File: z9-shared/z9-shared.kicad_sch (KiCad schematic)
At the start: 0 parts

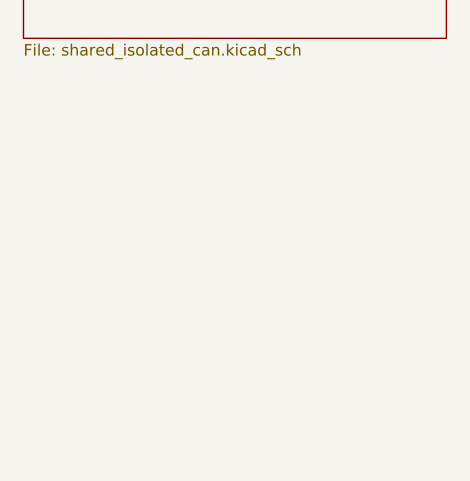
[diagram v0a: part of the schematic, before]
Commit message: Add shared_ism330dhcx schematic and update project configuration - Buzzer chaNGES 3.3v BEADS ANDCAPS - Created a new schematic file for the shared_ism330dhcx component. - Updated the z9-shared project configuration to change the annotation start number from 950 to 700. - Added the shared_ism330dhcx sheet to the main schematic with relevant properties and instances.
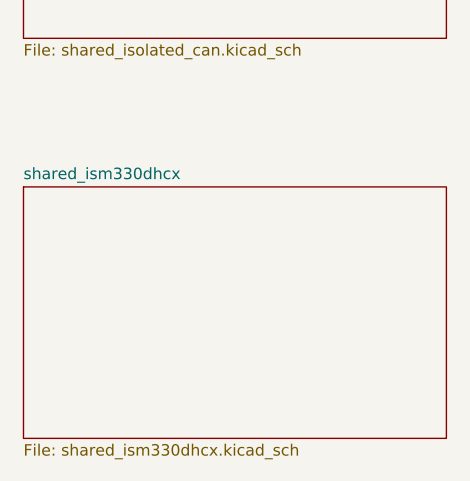
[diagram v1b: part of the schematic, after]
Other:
- added sheet shared_ism330dhcx (shared_ism330dhcx.kicad_sch)
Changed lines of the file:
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@@
+		)
+	)
+	(sheet
+		(at 36.83 147.32)
+		(size 46.99 27.94)
+		(exclude_from_sim no)
+		(in_bom yes)
+		(on_board yes)
+		(dnp no)
+		(fields_autoplaced yes)
+		(stroke
+			(width 0.1524)
+			(type solid)
+		)
+		(fill
+			(color 0 0 0 0.0000)
+		)
+		(property "Sheetname" "shared_ism330dhcx"
+			(at 36.83 146.6084 0)
+			(effects
+				(font
+					(size 1.27 1.27)
+				)
+				(justify left bottom)
+			)
+		)
+		(property "Sheetfile" "shared_ism330dhcx.kicad_sch"
+			(at 36.83 175.8446 0)
+			(effects
+				(font
+					(size 1.27 1.27)
+				)
+				(justify left top)
+			)
+		)
+		(instances
+			(project "z9-shared"
+				(path "/09e08bdc-786f-4949-8afc-e02ddbe0502e"
+					(page "750")
+				)
+			)
 		)
 	)

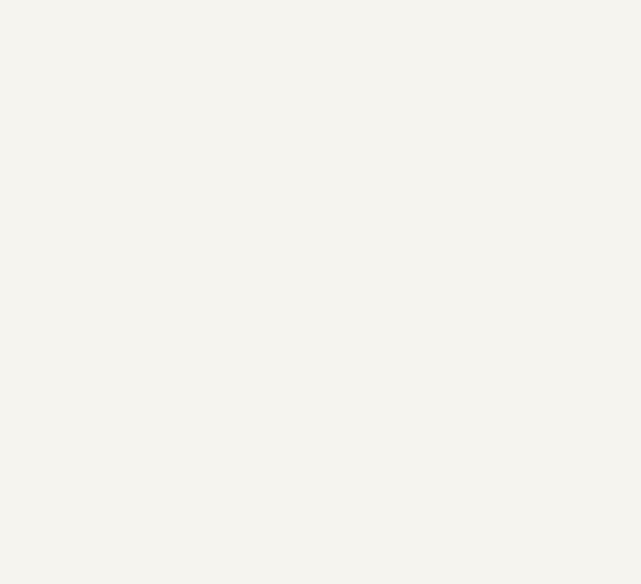
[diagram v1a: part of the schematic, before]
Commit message: Update schematic and project settings for shared components
- Changed the starting annotation number from 700 to 975 in the project configuration.
- Added a new shared schematic sheet named "shared_isolated_can_ps" with relevant properties and instances.
- Included a cautionary text in the schematic to avoid moving components and reannotating to prevent loss of links.
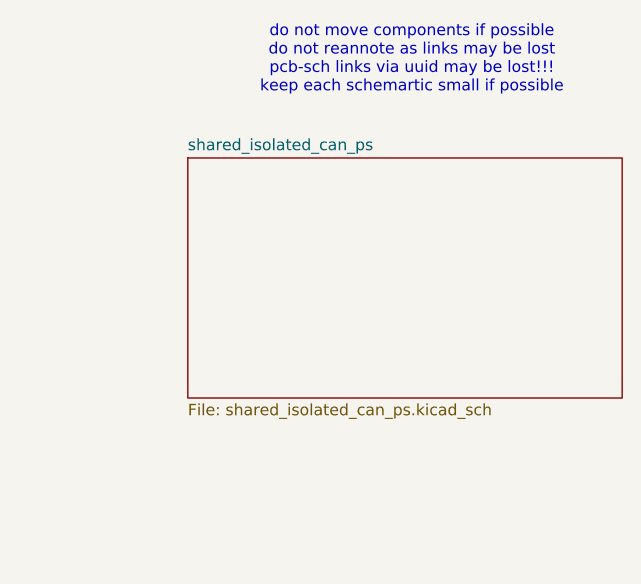
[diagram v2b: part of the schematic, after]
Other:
- added sheet shared_isolated_can_ps (shared_isolated_can_ps.kicad_sch)
- note added: "do not move components if possible do not reannote as links may be lost pcb-sch links via uuid may be lost!!! keep each schemartic small if possible"
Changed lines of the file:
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@@
 	(generator_version "9.0")
 	(paper "A4")
+	(text "do not move components if possible \ndo not reannote as links may be lost\npcb-sch links via uuid may be lost!!!\nkeep each schemartic small if possible "
+		(exclude_from_sim no)
+		(at 169.672 20.828 0)
+		(effects
+			(font
+				(size 1.27 1.27)
+			)
+		)
+	)
 	(no_connect
 		(at 83.82 114.3)
@@
 				)
 			)
+		)
+	)
+	(sheet
+		(at 144.78 31.75)
+		(size 48.26 26.67)
+		(exclude_from_sim no)
+		(in_bom yes)
+		(on_board yes)
+		(dnp no)
+		(fields_autoplaced yes)
+		(stroke
+			(width 0.1524)
+			(type solid)
+		)
+		(fill
+			(color 0 0 0 0.0000)
+		)
+		(property "Sheetname" "shared_isolated_can_ps"
+			(at 144.78 31.0384 0)
+			(effects
+				(font
+					(size 1.27 1.27)
+				)
+				(justify left bottom)
+			)
+		)
+		(property "Sheetfile" "shared_isolated_can_ps.kicad_sch"
+			(at 144.78 59.0046 0)
+			(effects
+				(font
+					(size 1.27 1.27)
+				)
+				(justify left top)
+			)
+		)
+		(instances
+			(project "z9-shared"
+				(path "/09e08bdc-786f-4949-8afc-e02ddbe0502e"
+					(page "7")
+				)
+			)

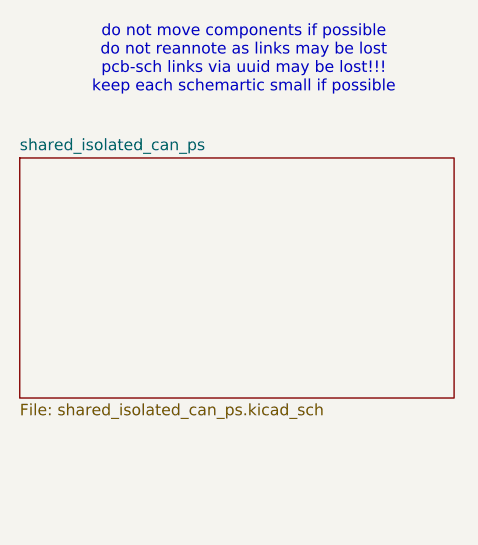
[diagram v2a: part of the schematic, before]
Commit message: Add no-connect pins and ISO power pins to the schematic for shared components
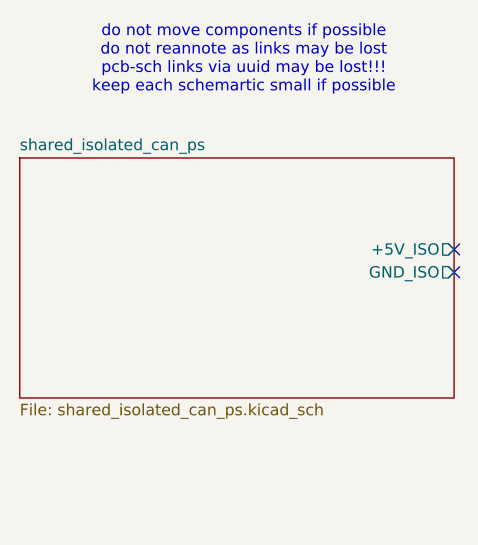
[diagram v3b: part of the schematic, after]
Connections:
- no-connect marks 10 -> 12
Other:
- sheet shared_isolated_can_ps ports: added +5V_ISO, GND_ISO; removed none
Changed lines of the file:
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@@
+	)
+	(no_connect
+		(at 193.04 41.91)
 	)
 	(no_connect
@@
 	(no_connect
 		(at 36.83 43.18)
+	)
+	(no_connect
+		(at 193.04 44.45)
 	)
 	(no_connect
@@
 			)
 		)
+		(pin "+5V_ISO" output
+			(at 193.04 41.91 0)
+			(effects
+				(font
+					(size 1.27 1.27)
+				)
+				(justify right)
+			)
+		)
+		(pin "GND_ISO" output
+			(at 193.04 44.45 0)
+			(effects
+				(font
+					(size 1.27 1.27)
+				)
+				(justify right)
+			)
+		)

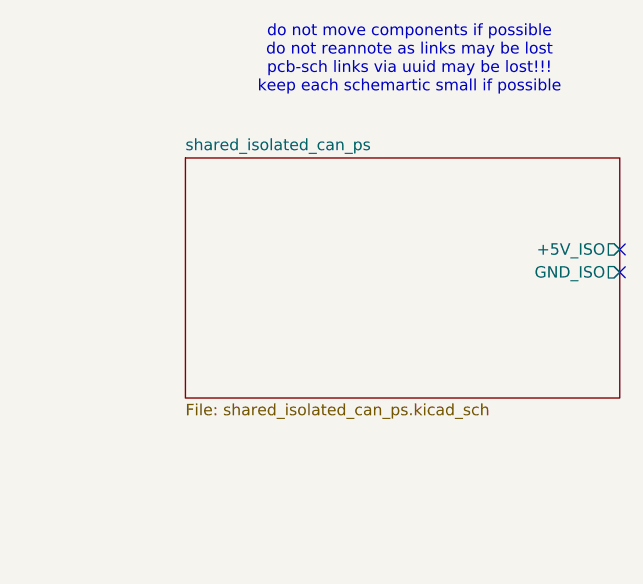
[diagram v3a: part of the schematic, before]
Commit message: Remove unused components and adjust annotation start number in project files
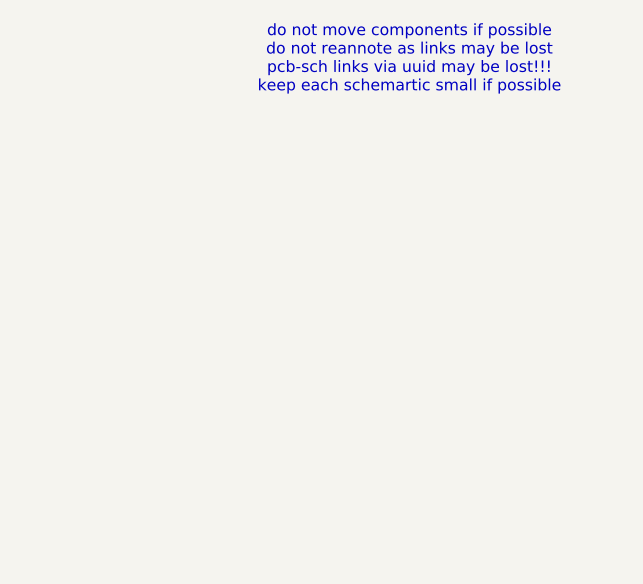
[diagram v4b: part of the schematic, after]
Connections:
- no-connect marks 12 -> 10
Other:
- removed sheet shared_isolated_can_ps
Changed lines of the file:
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@@
-	)
-	(no_connect
-		(at 193.04 41.91)
 	)
 	(no_connect
@@
 	(no_connect
 		(at 36.83 43.18)
-	)
-	(no_connect
-		(at 193.04 44.45)
 	)
 	(no_connect
@@
 				)
 			)
-		)
-	)
-	(sheet
-		(at 144.78 31.75)
-		(size 48.26 26.67)
-		(exclude_from_sim no)
-		(in_bom yes)
-		(on_board yes)
-		(dnp no)
-		(fields_autoplaced yes)
-		(stroke
-			(width 0.1524)
-			(type solid)
-		)
-		(fill
-			(color 0 0 0 0.0000)
-		)
-		(property "Sheetname" "shared_isolated_can_ps"
-			(at 144.78 31.0384 0)
-			(effects
-				(font
-					(size 1.27 1.27)
-				)
-				(justify left bottom)
-			)
-		)
-		(property "Sheetfile" "shared_isolated_can_ps.kicad_sch"
-			(at 144.78 59.0046 0)
-			(effects
-				(font
-					(size 1.27 1.27)
-				)
-				(justify left top)
-			)
-		)
-		(pin "+5V_ISO" output
-			(at 193.04 41.91 0)
-			(effects
-				(font
-					(size 1.27 1.27)
-				)
-				(justify right)
-			)
-		)
-		(pin "GND_ISO" output
-			(at 193.04 44.45 0)
-			(effects
-				(font
-					(size 1.27 1.27)
-				)
-				(justify right)
-			)
-		)
-		(instances
-			(project "z9-shared"
-				(path "/09e08bdc-786f-4949-8afc-e02ddbe0502e"
-					(page "7")
-				)
-			)

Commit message: x
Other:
- added sheet shared_usbc_esp32 (shared_usbc_esp32.kicad_sch)
- sheet shared_ism330dhcx ports: added ISM_CS, ISM_INT1, ISM_INT2, ISM_SCK, ISM_SDI, ISM_SDO; removed none
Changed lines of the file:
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@@
+	)
+	(sheet
+		(at 96.52 31.75)
+		(size 45.72 26.67)
+		(exclude_from_sim no)
+		(in_bom yes)
+		(on_board yes)
+		(dnp no)
+		(fields_autoplaced yes)
+		(stroke
+			(width 0.1524)
+			(type solid)
+		)
+		(fill
+			(color 0 0 0 0.0000)
+		)
+		(property "Sheetname" "shared_usbc_esp32"
+			(at 96.52 31.0384 0)
+			(effects
+				(font
+					(size 1.27 1.27)
+				)
+				(justify left bottom)
+			)
+		)
+		(property "Sheetfile" "shared_usbc_esp32.kicad_sch"
+			(at 96.52 59.0046 0)
+			(effects
+				(font
+					(size 1.27 1.27)
+				)
+				(justify left top)
+			)
+		)
+		(instances
+			(project "z9-shared"
+				(path "/09e08bdc-786f-4949-8afc-e02ddbe0502e"
+					(page "825")
+				)
+			)
+		)
 	)
 	(sheet
@@
 			)
 		)
+		(pin "ISM_CS" input
+			(at 36.83 153.67 180)
+			(effects
+				(font
+					(size 1.27 1.27)
+				)
+				(justify left)
+			)
+		)
+		(pin "ISM_INT1" input
+			(at 36.83 167.64 180)
+			(effects
+				(font
+					(size 1.27 1.27)
+				)
+				(justify left)
+			)
+		)
+		(pin "ISM_INT2" input
+			(at 36.83 170.18 180)
+			(effects
+				(font
+					(size 1.27 1.27)
+				)
+				(justify left)
+			)
+		)
+		(pin "ISM_SCK" input
+			(at 36.83 157.48 180)
+			(effects
+				(font
+					(size 1.27 1.27)
+				)
+				(justify left)
+			)
+		)
+		(pin "ISM_SDI" input
+			(at 36.83 160.02 180)
+			(effects
+				(font
+					(size 1.27 1.27)
+				)
+				(justify left)
+			)
+		)
+		(pin "ISM_SDO" input
+			(at 36.83 162.56 180)
+			(effects
+				(font
+					(size 1.27 1.27)
+				)
+				(justify left)
+			)
+		)

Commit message: pre kicad update
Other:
- added sheet shared_5V_LMR54410 (shared_5V_LMR54410.kicad_sch)
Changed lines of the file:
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@@
+		)
+	)
+	(sheet
+		(at 96.52 71.12)
+		(size 45.72 26.67)
+		(exclude_from_sim no)
+		(in_bom yes)
+		(on_board yes)
+		(dnp no)
+		(fields_autoplaced yes)
+		(stroke
+			(width 0.1524)
+			(type solid)
+		)
+		(fill
+			(color 0 0 0 0.0000)
+		)
+		(property "Sheetname" "shared_5V_LMR54410"
+			(at 96.52 70.4084 0)
+			(effects
+				(font
+					(size 1.27 1.27)
+				)
+				(justify left bottom)
+			)
+		)
+		(property "Sheetfile" "shared_5V_LMR54410.kicad_sch"
+			(at 96.52 98.3746 0)
+			(effects
+				(font
+					(size 1.27 1.27)
+				)
+				(justify left top)
+			)
+		)
+		(instances
+			(project "z9-shared"
+				(path "/09e08bdc-786f-4949-8afc-e02ddbe0502e"
+					(page "600")
+				)
+			)
 		)
 	)

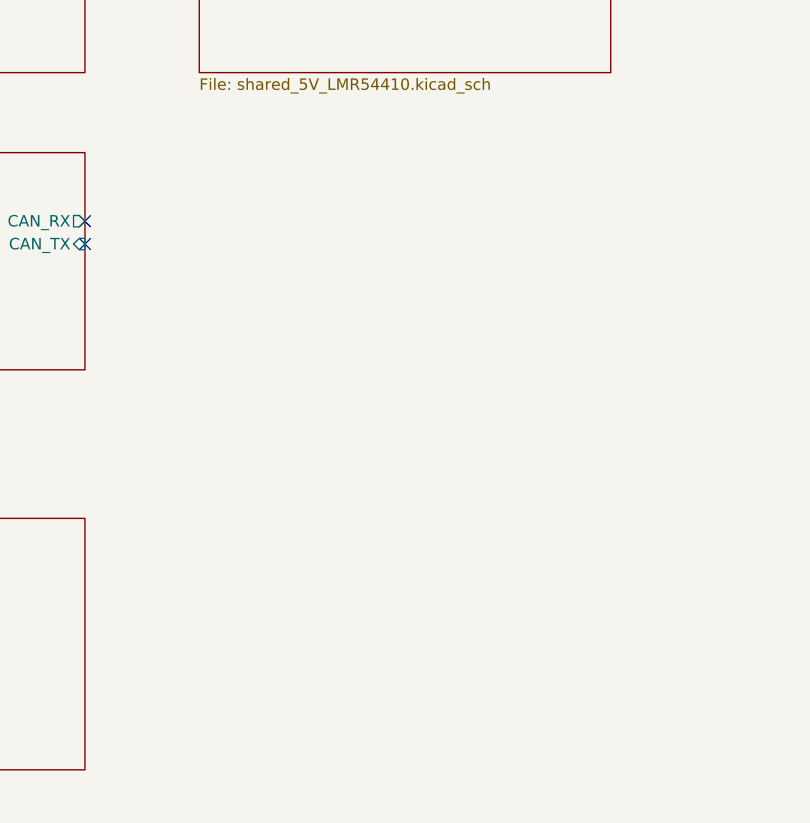
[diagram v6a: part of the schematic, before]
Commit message: new fuse and ideal diode
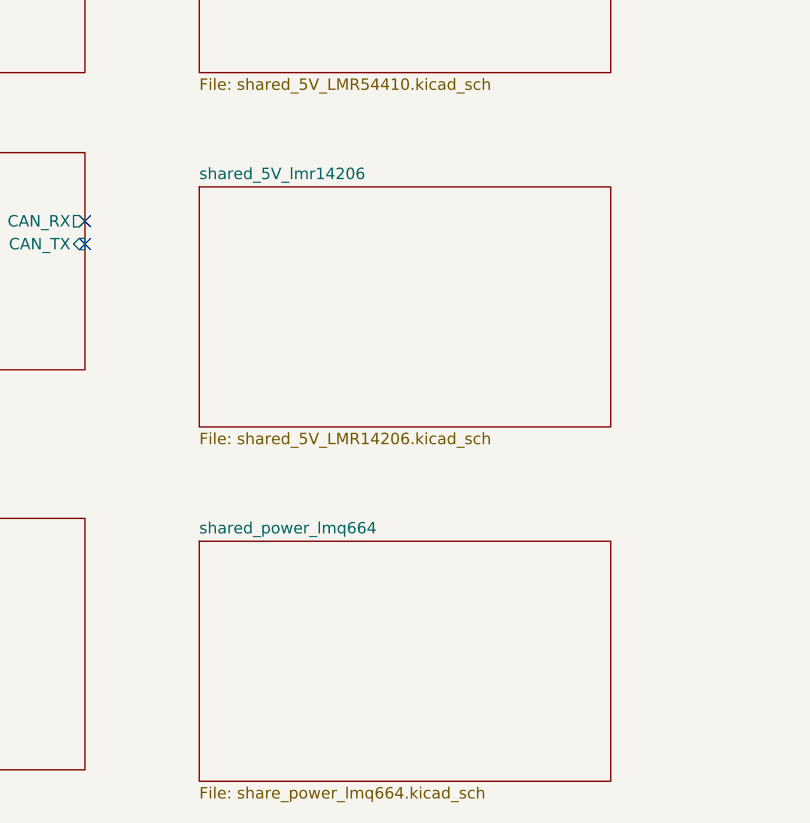
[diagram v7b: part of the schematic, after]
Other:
- added sheet shared_5V_lmr14206 (shared_5V_LMR14206.kicad_sch)
- added sheet shared_power_lmq664 (share_power_lmq664.kicad_sch)
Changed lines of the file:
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@@
+	)
+	(sheet
+		(at 96.52 149.86)
+		(size 45.72 26.67)
+		(exclude_from_sim no)
+		(in_bom yes)
+		(on_board yes)
+		(dnp no)
+		(fields_autoplaced yes)
+		(stroke
+			(width 0.1524)
+			(type solid)
+		)
+		(fill
+			(color 0 0 0 0.0000)
+		)
+		(property "Sheetname" "shared_power_lmq664"
+			(at 96.52 149.1484 0)
+			(effects
+				(font
+					(size 1.27 1.27)
+				)
+				(justify left bottom)
+			)
+		)
+		(property "Sheetfile" "share_power_lmq664.kicad_sch"
+			(at 96.52 177.1146 0)
+			(effects
+				(font
+					(size 1.27 1.27)
+				)
+				(justify left top)
+			)
+		)
+		(instances
+			(project "z9-shared"
+				(path "/09e08bdc-786f-4949-8afc-e02ddbe0502e"
+					(page "9")
+				)
+			)
+		)
 	)
 	(sheet
@@
 				)
 			)
+		)
+	)
+	(sheet
+		(at 96.52 110.49)
+		(size 45.72 26.67)
+		(exclude_from_sim no)
+		(in_bom yes)
+		(on_board yes)
+		(dnp no)
+		(fields_autoplaced yes)
+		(stroke
+			(width 0.1524)
+			(type solid)
+		)
+		(fill
+			(color 0 0 0 0.0000)
+		)
+		(property "Sheetname" "shared_5V_lmr14206"
+			(at 96.52 109.7784 0)
+			(effects
+				(font
+					(size 1.27 1.27)
+				)
+				(justify left bottom)
+			)
+		)
+		(property "Sheetfile" "shared_5V_LMR14206.kicad_sch"
+			(at 96.52 137.7446 0)
+			(effects
+				(font
+					(size 1.27 1.27)
+				)
+				(justify left top)
+			)
+		)
+		(instances
+			(project "z9-shared"
+				(path "/09e08bdc-786f-4949-8afc-e02ddbe0502e"
+					(page "8")
+				)
+			)
